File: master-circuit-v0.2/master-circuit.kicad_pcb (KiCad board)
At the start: 4 copper layers, 70 x 86 mm, 254 parts, among them U6 20nF 5%, X2 24MHz

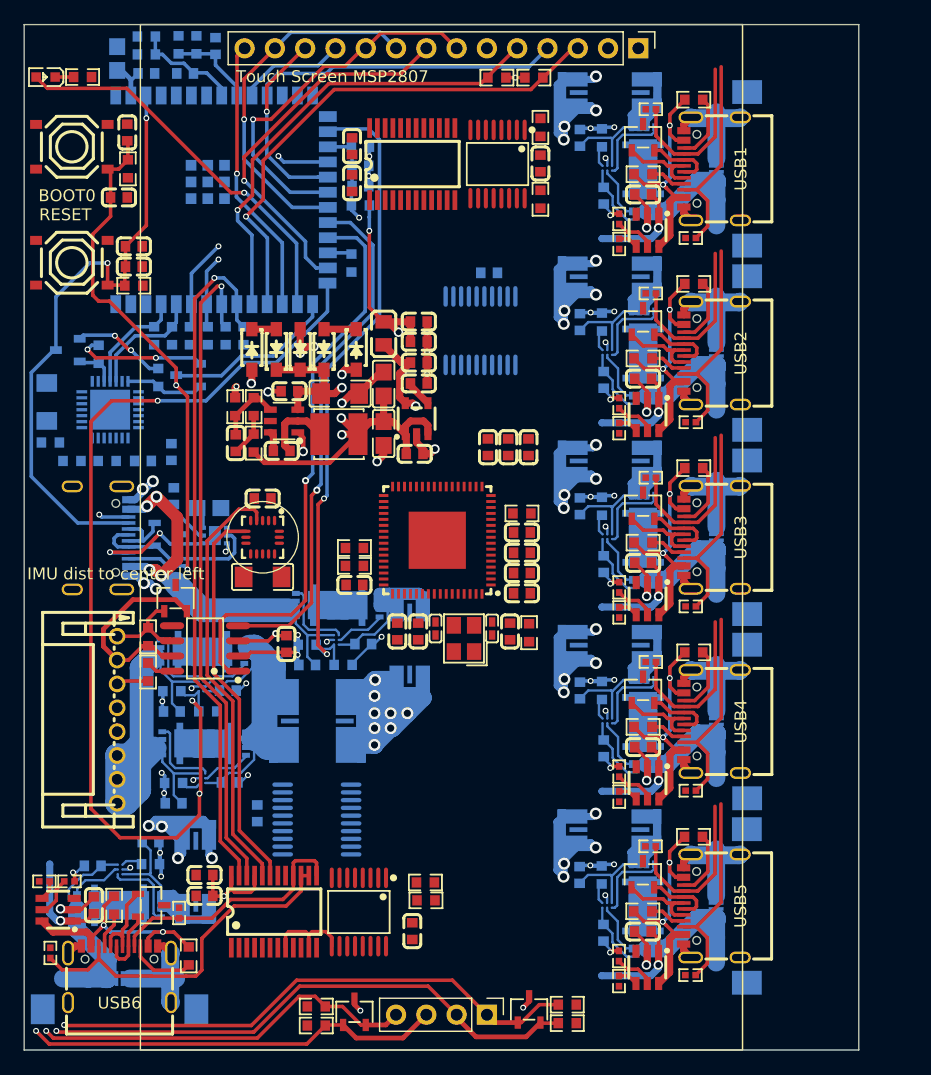
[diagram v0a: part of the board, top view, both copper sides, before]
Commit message: USB hub lines remaining.
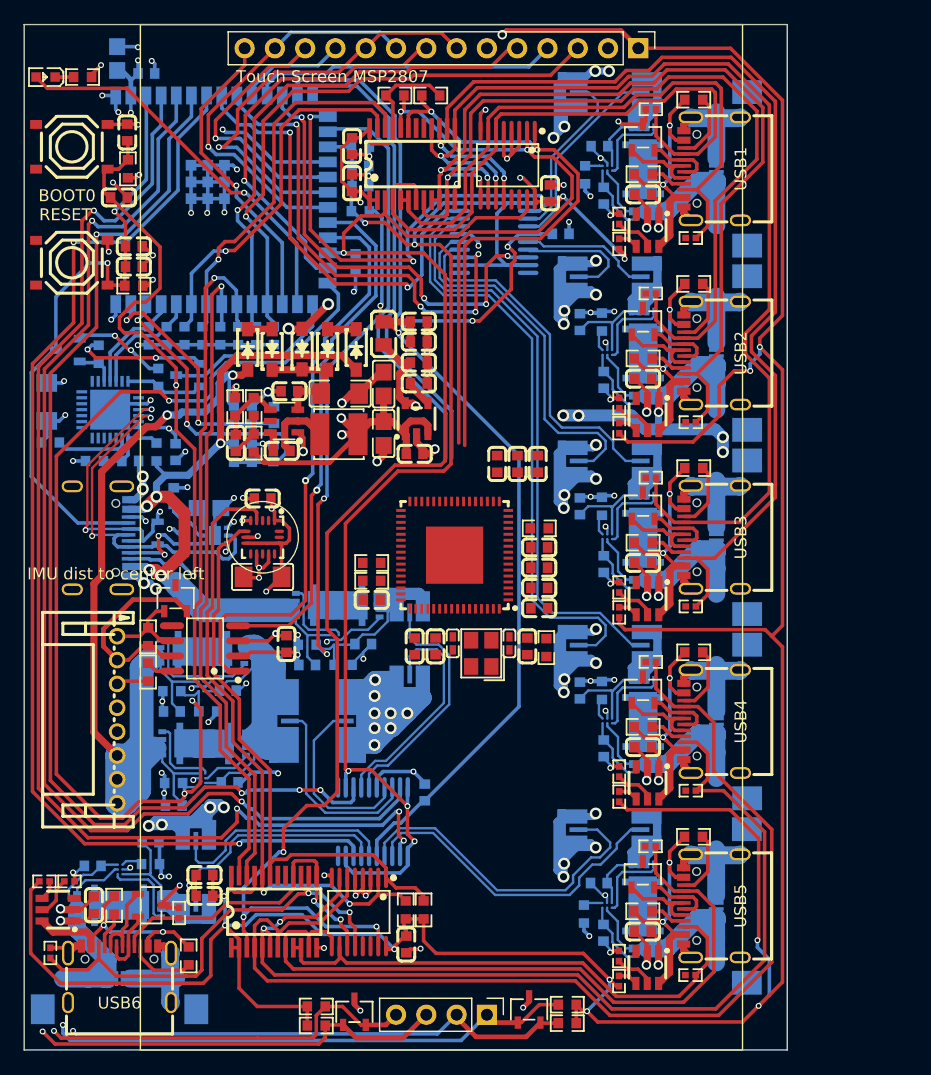
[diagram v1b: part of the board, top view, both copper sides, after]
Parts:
- R26, R27: moved to B.Cu
- moved R45 35.7 mm to (117.6, 93.0), turned to 90 degrees
- moved R47 34.6 mm to (119.1, 93.0), turned to -90 degrees
- moved C10 32.7 mm to (120.9, 93.0), turned to -90 degrees
- moved R38 31.4 mm to (119.1, 89.8)
- moved R48 31.4 mm to (117.6, 89.8)
- moved C11 31.3 mm to (121.0, 89.8)
- moved R27 30.7 mm to (120.9, 83.1), turned to -90 degrees
- moved R26 29.6 mm to (119.5, 83.1), turned to -90 degrees
- moved R58 15.0 mm to (131.1, 63.0), turned to 180 degrees
- moved C38 14.2 mm to (133.6, 121.4)
- moved R53 9.58 mm to (134.1, 63.0), turned to 0 degrees
- moved U11 7.85 mm to (139.4, 74.9), turned to 180 degrees
- moved R40 7.13 mm to (111.1, 92.8), turned to 90 degrees
- moved C39 6.84 mm to (145.0, 74.5)
- moved U16 4.70 mm to (129.2, 123.8), turned to 90 degrees
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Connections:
- R49 pad 2: CONNECTx -> PRTPWR1
- R54 pad 2: CONNECTx -> PRTPWR2
- R57 pad 2: CONNECTx -> PRTPWR3
- R63 pad 2: CONNECTx -> PRTPWR4
- R69 pad 2: CONNECTx -> PRTPWR5
- R75 pad 2: CONNECTx -> PRTPWR6
- U1 pad 12: VCC_CURRENT -> SERVO2_CURRENT
- U1 pad 15: SERVO3_CURRENT -> SERVO1_CURRENT
- U1 pad 38: SERVO2_CURRENT -> VBUS_VOLTAGE
- U1 pad 39: SERVO1_CURRENT -> BATTERY_VOLTAGE
- U1 pad 4: SERVO4_CURRENT -> SERVO5_CURRENT
- U1 pad 5: SERVO5_CURRENT -> BATTERY_CURRENT
- U1 pad 6: SERVO6_CURRENT -> VBUS_CURRENT
- U1 pad 7: SERVO7_CURRENT -> SERVO6_CURRENT
- U1 pad 8: VBUS_VOLTAGE -> SERVO4_CURRENT
- U1 pad 9: BATTERY_VOLTAGE -> SERVO3_CURRENT
- U11 pad 17: +Probe-4 -> -Probe-4
- U11 pad 18: -Probe-4 -> +Probe-4
- U11 pad 3: -Probe-1 -> +Probe-1
- U11 pad 4: +Probe-1 -> -Probe-1
- U11 pad 6: +Probe-2 -> -Probe-2
- U11 pad 7: -Probe-2 -> +Probe-2
- U16 pad 13: SERVO7_CURRENT -> VBUS_CURRENT
- U16 pad 14: -Probe-7 -> +Probe-7
- U16 pad 15: +Probe-7 -> -Probe-7
- U16 pad 19: VCC_CURRENT -> BATTERY_CURRENT
- U21 pad C2: CONNECTx -> PRTPWR1
- U22 pad C2: CONNECTx -> PRTPWR2
- U25 pad C2: CONNECTx -> PRTPWR3
- U27 pad C2: CONNECTx -> PRTPWR4
- U29 pad C2: CONNECTx -> PRTPWR5
- U31 pad C2: CONNECTx -> PRTPWR6
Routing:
- net 3V3: track 27.8 -> 373.0 mm, vias 4 -> 26
- net 5V: track 75.9 -> 258.2 mm, vias 8 -> 12
- net NRESET_ALL_MULTIPLEXERS: track 2.02 -> 115.6 mm, vias 0 -> 4
- net GND: track 177.2 -> 289.7 mm, vias 58 -> 99
- net REFERENCE: track 8.24 -> 114.7 mm, vias 1 -> 5
- net SERVO5_CURRENT: track 0.00 -> 103.5 mm, vias 0 -> 4
- net BATTERY_CURRENT: track 0.00 -> 99.7 mm, vias 0 -> 2
- net SERVO6_CURRENT: track 0.00 -> 96.8 mm, vias 0 -> 2
- net VBUS_CURRENT: track 0.00 -> 94.0 mm, vias 0 -> 4
- net SERVO4_BOOT0: track 14.1 -> 94.6 mm
- net SERVO3_BOOT0: track 14.1 -> 91.9 mm, vias 0 -> 2
- net SERVO3_NRST: track 17.1 -> 93.7 mm, vias 0 -> 2
- net 3V3A: track 15.8 -> 88.4 mm, vias 2 -> 4
- net SERVO4_NRST: track 17.1 -> 82.9 mm, vias 0 -> 2
- net SERVO2_BOOT0: track 14.1 -> 71.1 mm, vias 0 -> 2
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- added copper zone on In1.Cu, net 3V3
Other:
- board size 70 x 86 mm -> 64 x 86 mm

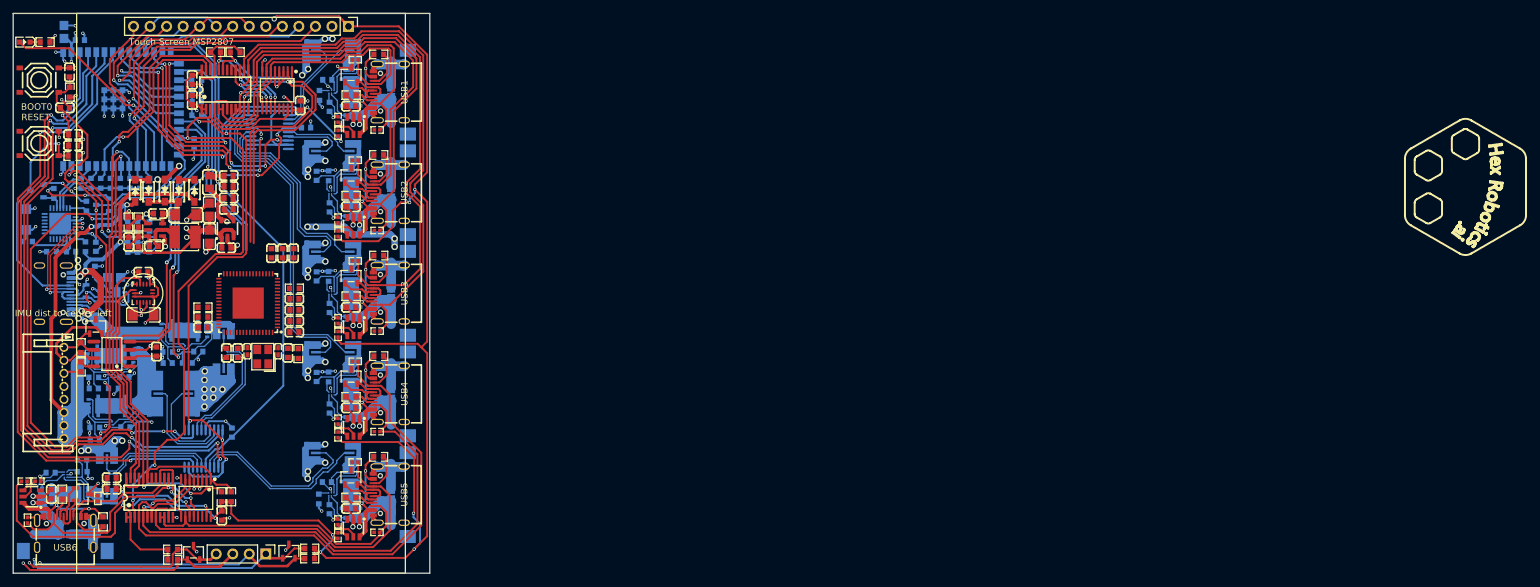
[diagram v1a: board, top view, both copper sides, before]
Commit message: Finish wiring master circuit v0.2.
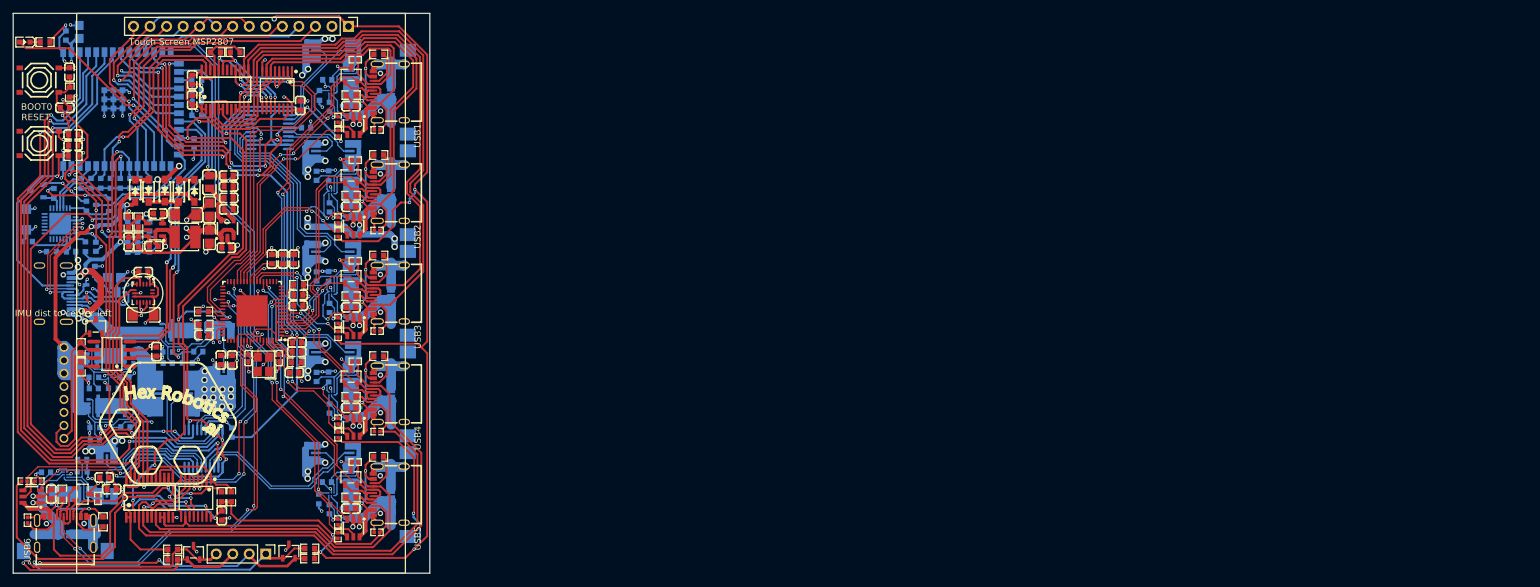
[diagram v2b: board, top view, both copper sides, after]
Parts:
- U19: moved to B.Cu
- moved C70 4.76 mm to (143.6, 109.0)
- moved C65 3.21 mm to (143.2, 112.2), turned to 180 degrees
- moved C3 2.35 mm to (110.2, 59.9)
- moved C2 2.26 mm to (108.1, 60.4), turned to -90 degrees
- moved C71 1.65 mm to (143.6, 107.5)
- moved C66 1.39 mm to (133.7, 110.2)
- moved C67 1.39 mm to (131.9, 110.2)
- moved R50 1.38 mm to (143.5, 110.6), turned to 0 degrees
- moved U24 1.34 mm to (136.7, 102.7)
- moved X2 1.17 mm to (138.4, 110.9)
- moved C68 1.16 mm to (129.3, 106.4), turned to 180 degrees
- moved R51 1.16 mm to (129.3, 104.8)
- moved C43 1.13 mm to (114.0, 128.3)
- moved C64 1.06 mm to (140.8, 110.0), turned to -90 degrees
- moved C69 1.06 mm to (136.1, 110.0)
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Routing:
- net GND: track 289.7 -> 366.3 mm, vias 99 -> 118
- net PRTPWR6: track 1.91 -> 69.9 mm, vias 0 -> 5
- net nOCS6: track 1.68 -> 68.5 mm, vias 0 -> 4
- net USBDN6_D-: track 6.92 -> 71.7 mm, vias 0 -> 2
- net USBDN6_D+: track 5.66 -> 69.9 mm, vias 0 -> 2
- net USBDN1_D+: track 5.66 -> 53.2 mm, vias 0 -> 2
- net USBDN1_D-: track 6.92 -> 52.7 mm, vias 0 -> 2
- net nOCS5: track 1.68 -> 46.4 mm, vias 0 -> 2
- net PRTPWR5: track 1.61 -> 46.1 mm, vias 0 -> 3
- net PRTPWR1: track 1.46 -> 42.7 mm, vias 0 -> 3
- net USBDN5_D+: track 5.66 -> 41.4 mm, vias 0 -> 2
- net USBDN5_D-: track 6.92 -> 40.8 mm, vias 0 -> 2
- net USBDN2_D+: track 5.66 -> 39.2 mm
- net nOCS1: track 1.68 -> 33.4 mm, vias 0 -> 2
- net USBDN2_D-: track 6.92 -> 37.9 mm
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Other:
- board text added: "GND 10x --- 10x VCC"

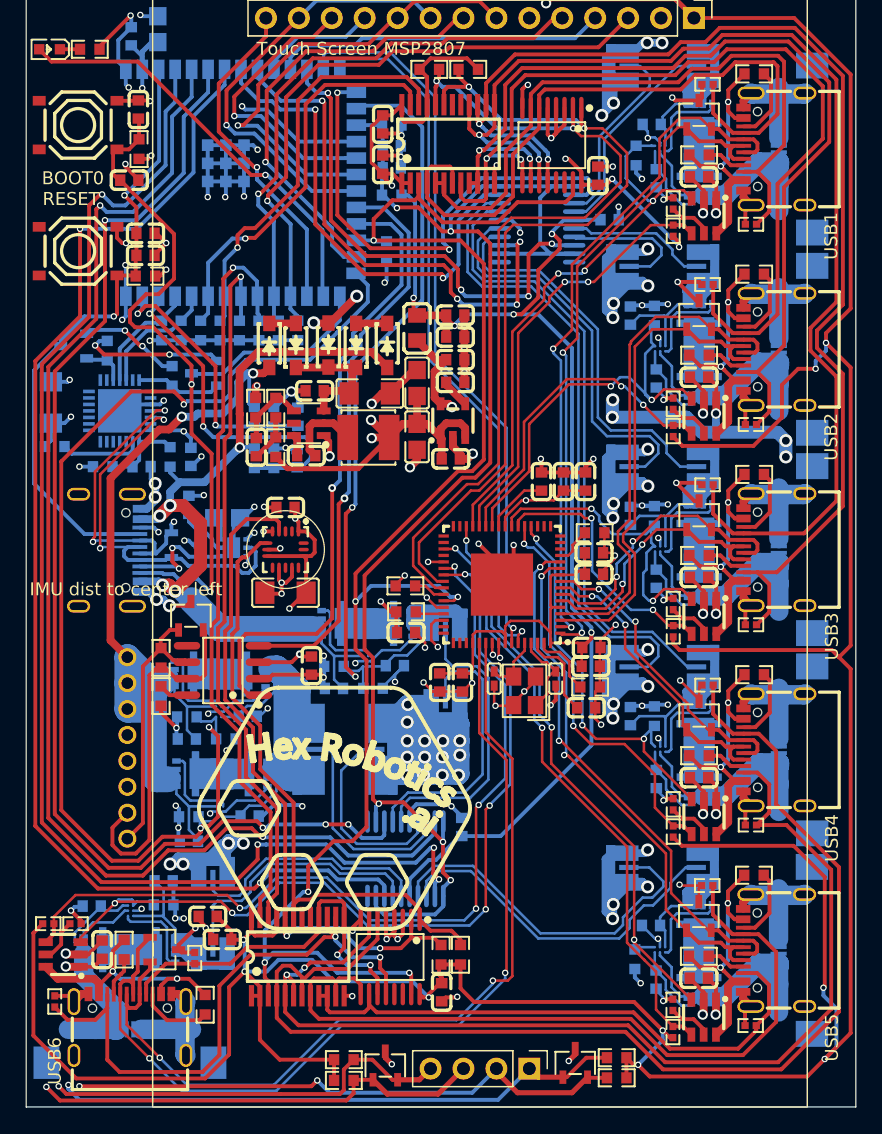
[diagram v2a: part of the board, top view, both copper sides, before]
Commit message: Finish extender cable circuit.
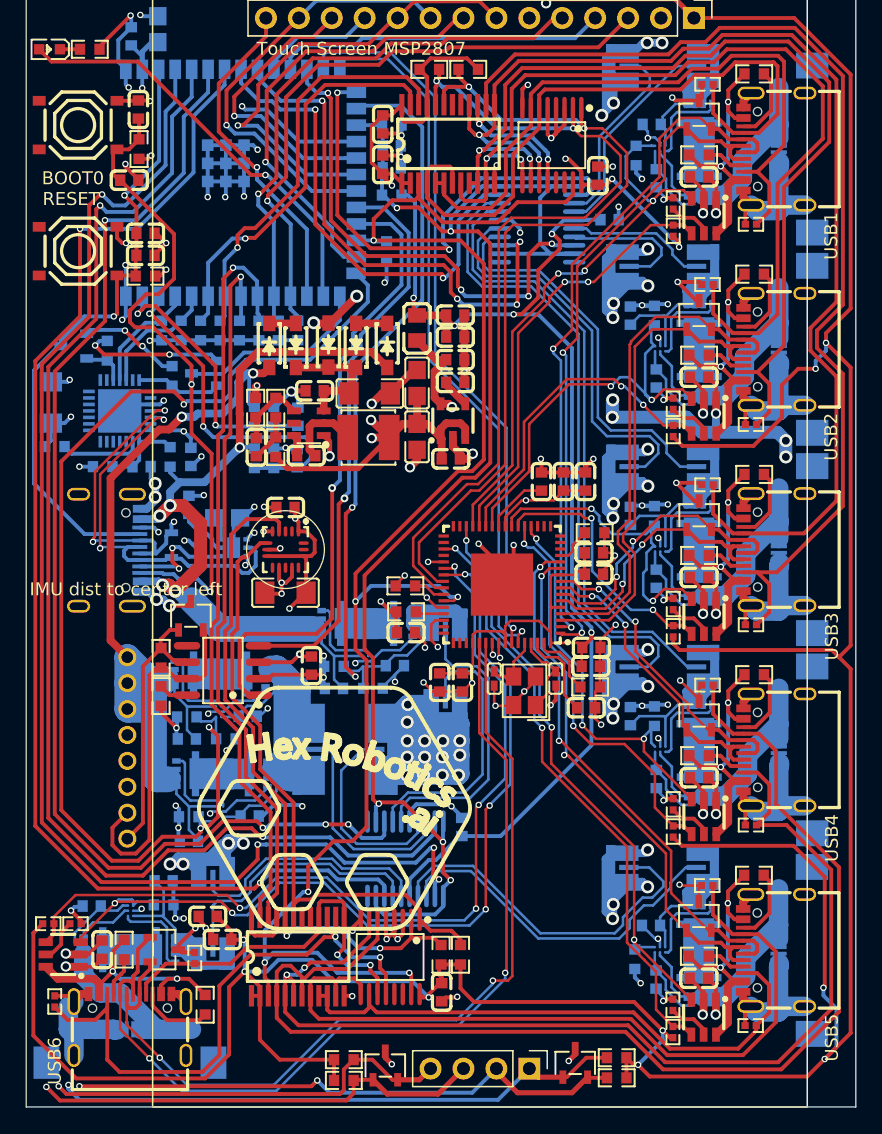
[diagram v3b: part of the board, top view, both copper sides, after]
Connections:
- FPC1 pad 1: GND -> /servo-usb-connector/VCCx
- FPC1 pad 10: GND -> /servo-usb-connector/VCCx
- FPC1 pad 11: /servo-usb-connector/VCCx -> GND
- FPC1 pad 12: /servo-usb-connector/VCCx -> GND
- FPC1 pad 13: /servo-usb-connector/VCCx -> GND
- FPC1 pad 14: /servo-usb-connector/VCCx -> GND
- FPC1 pad 15: /servo-usb-connector/VCCx -> GND
- FPC1 pad 16: /servo-usb-connector/VCCx -> GND
- FPC1 pad 17: /servo-usb-connector/VCCx -> GND
- FPC1 pad 18: /servo-usb-connector/VCCx -> GND
- FPC1 pad 19: /servo-usb-connector/VCCx -> GND
- FPC1 pad 2: GND -> /servo-usb-connector/VCCx
- FPC1 pad 20: /servo-usb-connector/VCCx -> GND
- FPC1 pad 3: GND -> /servo-usb-connector/VCCx
- FPC1 pad 4: GND -> /servo-usb-connector/VCCx
- FPC1 pad 5: GND -> /servo-usb-connector/VCCx
- FPC1 pad 6: GND -> /servo-usb-connector/VCCx
- FPC1 pad 7: GND -> /servo-usb-connector/VCCx
- FPC1 pad 8: GND -> /servo-usb-connector/VCCx
- FPC1 pad 9: GND -> /servo-usb-connector/VCCx
- FPC2 pad 1: GND -> /servo-usb-connector1/VCCx
- FPC2 pad 10: GND -> /servo-usb-connector1/VCCx
- FPC2 pad 11: /servo-usb-connector1/VCCx -> GND
- FPC2 pad 12: /servo-usb-connector1/VCCx -> GND
- FPC2 pad 13: /servo-usb-connector1/VCCx -> GND
- FPC2 pad 14: /servo-usb-connector1/VCCx -> GND
- FPC2 pad 15: /servo-usb-connector1/VCCx -> GND
- FPC2 pad 16: /servo-usb-connector1/VCCx -> GND
- FPC2 pad 17: /servo-usb-connector1/VCCx -> GND
- FPC2 pad 18: /servo-usb-connector1/VCCx -> GND
- FPC2 pad 19: /servo-usb-connector1/VCCx -> GND
- FPC2 pad 2: GND -> /servo-usb-connector1/VCCx
- FPC2 pad 20: /servo-usb-connector1/VCCx -> GND
- FPC2 pad 3: GND -> /servo-usb-connector1/VCCx
- FPC2 pad 4: GND -> /servo-usb-connector1/VCCx
- FPC2 pad 5: GND -> /servo-usb-connector1/VCCx
- FPC2 pad 6: GND -> /servo-usb-connector1/VCCx
- FPC2 pad 7: GND -> /servo-usb-connector1/VCCx
- FPC2 pad 8: GND -> /servo-usb-connector1/VCCx
- FPC2 pad 9: GND -> /servo-usb-connector1/VCCx
- FPC3 pad 1: GND -> /servo-usb-connector2/VCCx
- FPC3 pad 10: GND -> /servo-usb-connector2/VCCx
- FPC3 pad 11: /servo-usb-connector2/VCCx -> GND
- FPC3 pad 12: /servo-usb-connector2/VCCx -> GND
- FPC3 pad 13: /servo-usb-connector2/VCCx -> GND
- FPC3 pad 14: /servo-usb-connector2/VCCx -> GND
- FPC3 pad 15: /servo-usb-connector2/VCCx -> GND
- FPC3 pad 16: /servo-usb-connector2/VCCx -> GND
- FPC3 pad 17: /servo-usb-connector2/VCCx -> GND
- FPC3 pad 18: /servo-usb-connector2/VCCx -> GND
- FPC3 pad 19: /servo-usb-connector2/VCCx -> GND
- FPC3 pad 2: GND -> /servo-usb-connector2/VCCx
- FPC3 pad 20: /servo-usb-connector2/VCCx -> GND
- FPC3 pad 3: GND -> /servo-usb-connector2/VCCx
- FPC3 pad 4: GND -> /servo-usb-connector2/VCCx
- FPC3 pad 5: GND -> /servo-usb-connector2/VCCx
- FPC3 pad 6: GND -> /servo-usb-connector2/VCCx
- FPC3 pad 7: GND -> /servo-usb-connector2/VCCx
- FPC3 pad 8: GND -> /servo-usb-connector2/VCCx
- FPC3 pad 9: GND -> /servo-usb-connector2/VCCx
- FPC4 pad 1: GND -> /servo-usb-connector3/VCCx
- FPC4 pad 10: GND -> /servo-usb-connector3/VCCx
- FPC4 pad 11: /servo-usb-connector3/VCCx -> GND
- FPC4 pad 12: /servo-usb-connector3/VCCx -> GND
- FPC4 pad 13: /servo-usb-connector3/VCCx -> GND
- FPC4 pad 14: /servo-usb-connector3/VCCx -> GND
- FPC4 pad 15: /servo-usb-connector3/VCCx -> GND
- FPC4 pad 16: /servo-usb-connector3/VCCx -> GND
- FPC4 pad 17: /servo-usb-connector3/VCCx -> GND
- FPC4 pad 18: /servo-usb-connector3/VCCx -> GND
- FPC4 pad 19: /servo-usb-connector3/VCCx -> GND
- FPC4 pad 2: GND -> /servo-usb-connector3/VCCx
- FPC4 pad 20: /servo-usb-connector3/VCCx -> GND
- FPC4 pad 3: GND -> /servo-usb-connector3/VCCx
- FPC4 pad 4: GND -> /servo-usb-connector3/VCCx
- FPC4 pad 5: GND -> /servo-usb-connector3/VCCx
- FPC4 pad 6: GND -> /servo-usb-connector3/VCCx
- FPC4 pad 7: GND -> /servo-usb-connector3/VCCx
- FPC4 pad 8: GND -> /servo-usb-connector3/VCCx
- FPC4 pad 9: GND -> /servo-usb-connector3/VCCx
- FPC5 pad 1: GND -> /servo-usb-connector4/VCCx
- FPC5 pad 10: GND -> /servo-usb-connector4/VCCx
- FPC5 pad 11: /servo-usb-connector4/VCCx -> GND
- FPC5 pad 12: /servo-usb-connector4/VCCx -> GND
- FPC5 pad 13: /servo-usb-connector4/VCCx -> GND
- FPC5 pad 14: /servo-usb-connector4/VCCx -> GND
- FPC5 pad 15: /servo-usb-connector4/VCCx -> GND
- FPC5 pad 16: /servo-usb-connector4/VCCx -> GND
- FPC5 pad 17: /servo-usb-connector4/VCCx -> GND
- FPC5 pad 18: /servo-usb-connector4/VCCx -> GND
- FPC5 pad 19: /servo-usb-connector4/VCCx -> GND
- FPC5 pad 2: GND -> /servo-usb-connector4/VCCx
- FPC5 pad 20: /servo-usb-connector4/VCCx -> GND
- FPC5 pad 3: GND -> /servo-usb-connector4/VCCx
- FPC5 pad 4: GND -> /servo-usb-connector4/VCCx
- FPC5 pad 5: GND -> /servo-usb-connector4/VCCx
- FPC5 pad 6: GND -> /servo-usb-connector4/VCCx
- FPC5 pad 7: GND -> /servo-usb-connector4/VCCx
- FPC5 pad 8: GND -> /servo-usb-connector4/VCCx
- FPC5 pad 9: GND -> /servo-usb-connector4/VCCx
- FPC6 pad 1: GND -> /servo-usb-connector5/VCCx
- FPC6 pad 10: GND -> /servo-usb-connector5/VCCx
- FPC6 pad 11: /servo-usb-connector5/VCCx -> GND
- FPC6 pad 12: /servo-usb-connector5/VCCx -> GND
- FPC6 pad 13: /servo-usb-connector5/VCCx -> GND
- FPC6 pad 14: /servo-usb-connector5/VCCx -> GND
- FPC6 pad 15: /servo-usb-connector5/VCCx -> GND
- FPC6 pad 16: /servo-usb-connector5/VCCx -> GND
- FPC6 pad 17: /servo-usb-connector5/VCCx -> GND
- FPC6 pad 18: /servo-usb-connector5/VCCx -> GND
- FPC6 pad 19: /servo-usb-connector5/VCCx -> GND
- FPC6 pad 2: GND -> /servo-usb-connector5/VCCx
- FPC6 pad 20: /servo-usb-connector5/VCCx -> GND
- FPC6 pad 3: GND -> /servo-usb-connector5/VCCx
- FPC6 pad 4: GND -> /servo-usb-connector5/VCCx
- FPC6 pad 5: GND -> /servo-usb-connector5/VCCx
- FPC6 pad 6: GND -> /servo-usb-connector5/VCCx
- FPC6 pad 7: GND -> /servo-usb-connector5/VCCx
- FPC6 pad 8: GND -> /servo-usb-connector5/VCCx
- FPC6 pad 9: GND -> /servo-usb-connector5/VCCx
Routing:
- net GND: track 366.3 -> 367.6 mm
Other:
- board text added: "VCC|GND"
- board text removed: "GND 10x --- 10x VCC"
